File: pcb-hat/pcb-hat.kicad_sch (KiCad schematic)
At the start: 42 parts, among them U1 INA219AxD, U2 AOZ6605PI-1, U3 HTD Servo, U4 Vertical_Pi_Breakout, U5 Raspberry_Pi_Generic, U6 Power_Connector, U7 LM1084ISX-5.0_NOPB, U8 Horizontal_Pi_Breakout

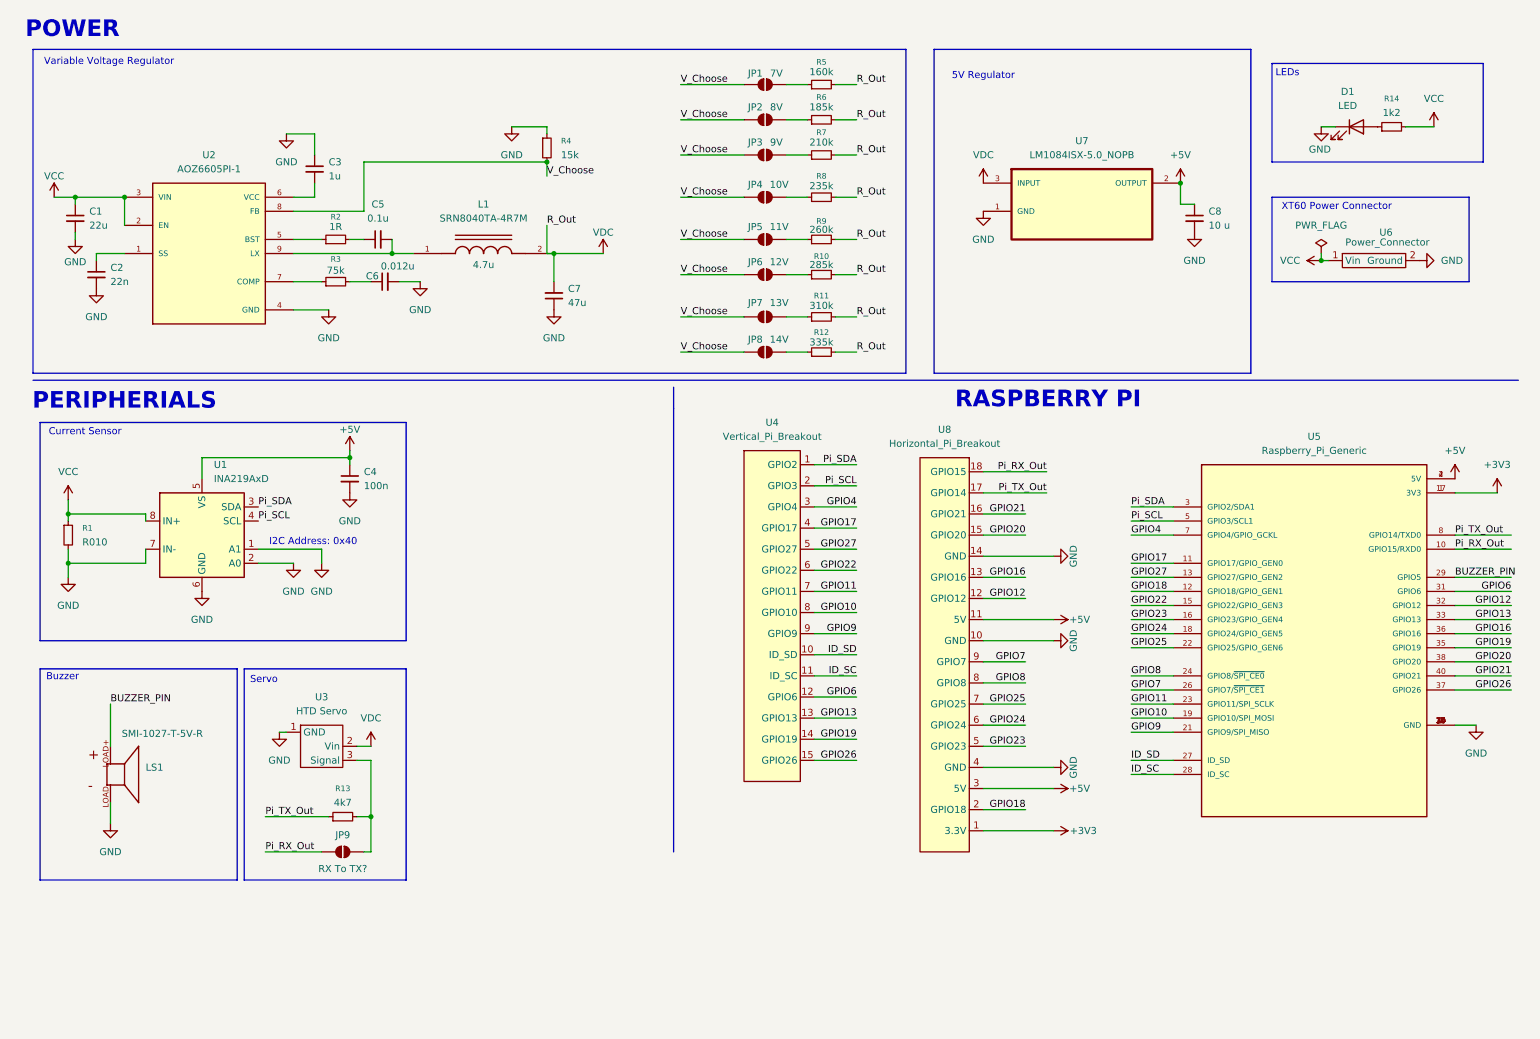
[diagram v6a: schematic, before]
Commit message: Don't short pwr to gnd for current sensor
Also use higher power rating for shunt
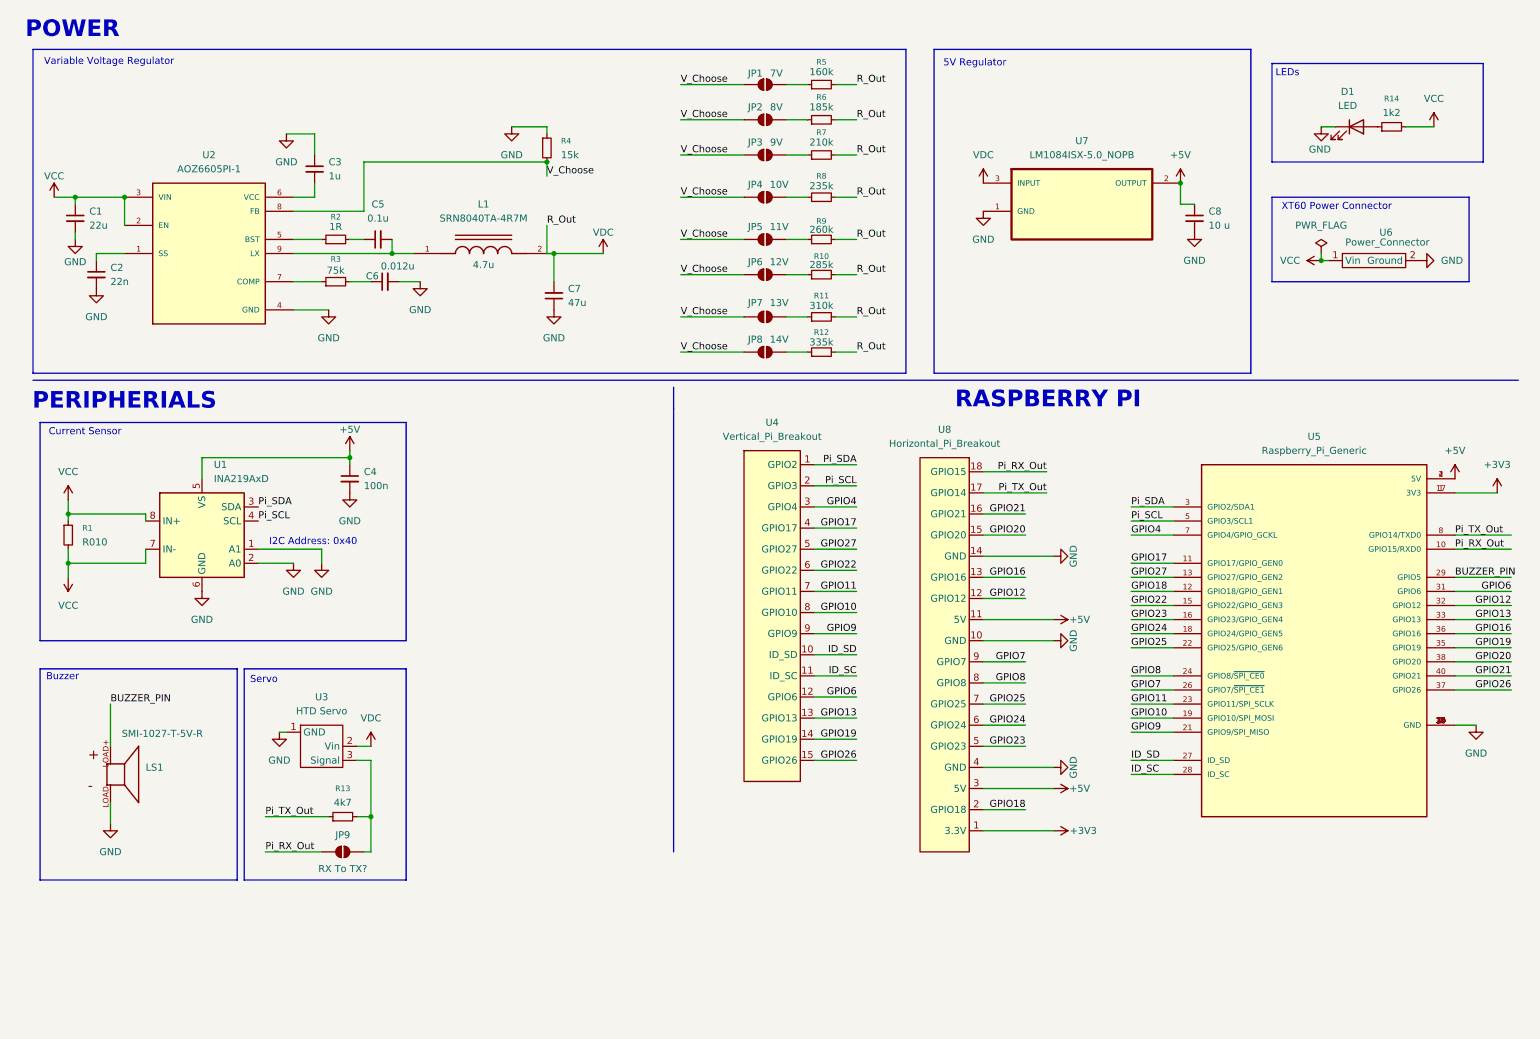
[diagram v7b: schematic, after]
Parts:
- R1: Digikey https://www.digikey.com/en/products/detail/susumu/RL0816T-R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 -> https://www.digikey.com/en/products/detail/yageo/PE0603FRE5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
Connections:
- net GND: no longer R1.2, U1.7 (IN-)
- net VCC: now also R1.2, U1.7 (IN-)
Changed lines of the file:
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@@
 	(text "5V Regulator\n"
 		(exclude_from_sim no)
-		(at 185.42 23.876 0)
+		(at 183.896 21.59 0)
 		(effects
 			(font
@@
 			)
 		)
-		(property "Datasheet" "https://www.susumu.co.jp/common/pdf/n_catalog_partition08_en.pdf"
+		(property "Datasheet" "https://mm.digikey.com/Volume0/opasdata/d220001/medias/docus/5343/PE_Series_DS.pdf"
 			(at 20.32 106.68 0)
 			(effects
@@
 			)
 		)
-		(property "Digikey" "https://www.digikey.com/en/products/detail/susumu/RL0816T-R010-F/2734741"
+		(property "Digikey" "https://www.digikey.com/en/products/detail/yageo/PE0603FRE570R01Z/17009517"
 			(at 20.32 106.68 0)
 			(effects
@@
 	)
 	(symbol
+		(lib_id "power:VCC")
+		(at 20.32 114.3 180)
+		(unit 1)
+		(exclude_from_sim no)
+		(in_bom yes)
+		(on_board yes)
+		(dnp no)
+		(fields_autoplaced yes)
+		(property "Reference" "#PWR03"
+			(at 20.32 110.49 0)
+			(effects
+				(font
+					(size 1.27 1.27)
+				)
+				(hide yes)
+			)
+		)
+		(property "Value" "VCC"
+			(at 20.32 119.38 0)
+			(effects
+				(font
+					(size 1.27 1.27)
+				)
+			)
+		)
+		(property "Footprint" ""
+			(at 20.32 114.3 0)
+			(effects
+				(font
+					(size 1.27 1.27)
+				)
+				(hide yes)
+			)
+		)
+		(property "Datasheet" ""
+			(at 20.32 114.3 0)
+			(effects
+				(font
+					(size 1.27 1.27)
+				)
+				(hide yes)
+			)
+		)
+		(property "Description" "Power symbol creates a global label with name \"VCC\""
+			(at 20.32 114.3 0)
+			(effects
+				(font
+					(size 1.27 1.27)
+				)
+				(hide yes)
+			)
+		)
+		(pin "1"
+		)
+		(instances
+			(project ""
+				(path "/a3c2d30d-0751-4de7-a899-3d89ad40795d"
+					(reference "#PWR03")
+					(unit 1)
+				)
+			)
+		)
+	)
+	(symbol
 		(lib_id "Device:C_Small")
 		(at 77.47 60.96 90)
@@
 					(unit 1)
 				)
-			)
-		)
-	)
-	(symbol
-		(lib_id "power:GND")
-		(at 20.32 114.3 0)
-		(unit 1)
-		(exclude_from_sim no)
-		(in_bom yes)
-		(on_board yes)
-		(dnp no)
-		(fields_autoplaced yes)
-		(property "Reference" "#PWR03"
-			(at 20.32 120.65 0)
-			(effects
-				(font
-					(size 1.27 1.27)
-				)
-				(hide yes)
-			)
-		)
-		(property "Value" "GND"
-			(at 20.32 119.38 0)
-			(effects
-				(font
-					(size 1.27 1.27)
-				)
-			)
-		)
-		(property "Footprint" ""
-			(at 20.32 114.3 0)
-			(effects
-				(font
-					(size 1.27 1.27)
-				)
-				(hide yes)
-			)
-		)
-		(property "Datasheet" ""
-			(at 20.32 114.3 0)
-			(effects
-				(font
-					(size 1.27 1.27)
-				)
-				(hide yes)
-			)
-		)
-		(property "Description" "Power symbol creates a global label with name \"GND\" , ground"
-			(at 20.32 114.3 0)
-			(effects
-				(font
-					(size 1.27 1.27)
-				)
-				(hide yes)
-			)
-		)
-		(pin "1"
-		)
-		(instances
-			(project ""
-				(path "/a3c2d30d-0751-4de7-a899-3d89ad40795d"
-					(reference "#PWR03")
-					(unit 1)
-				)

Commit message: Add mosfets, new led, and cleanup schematic some more
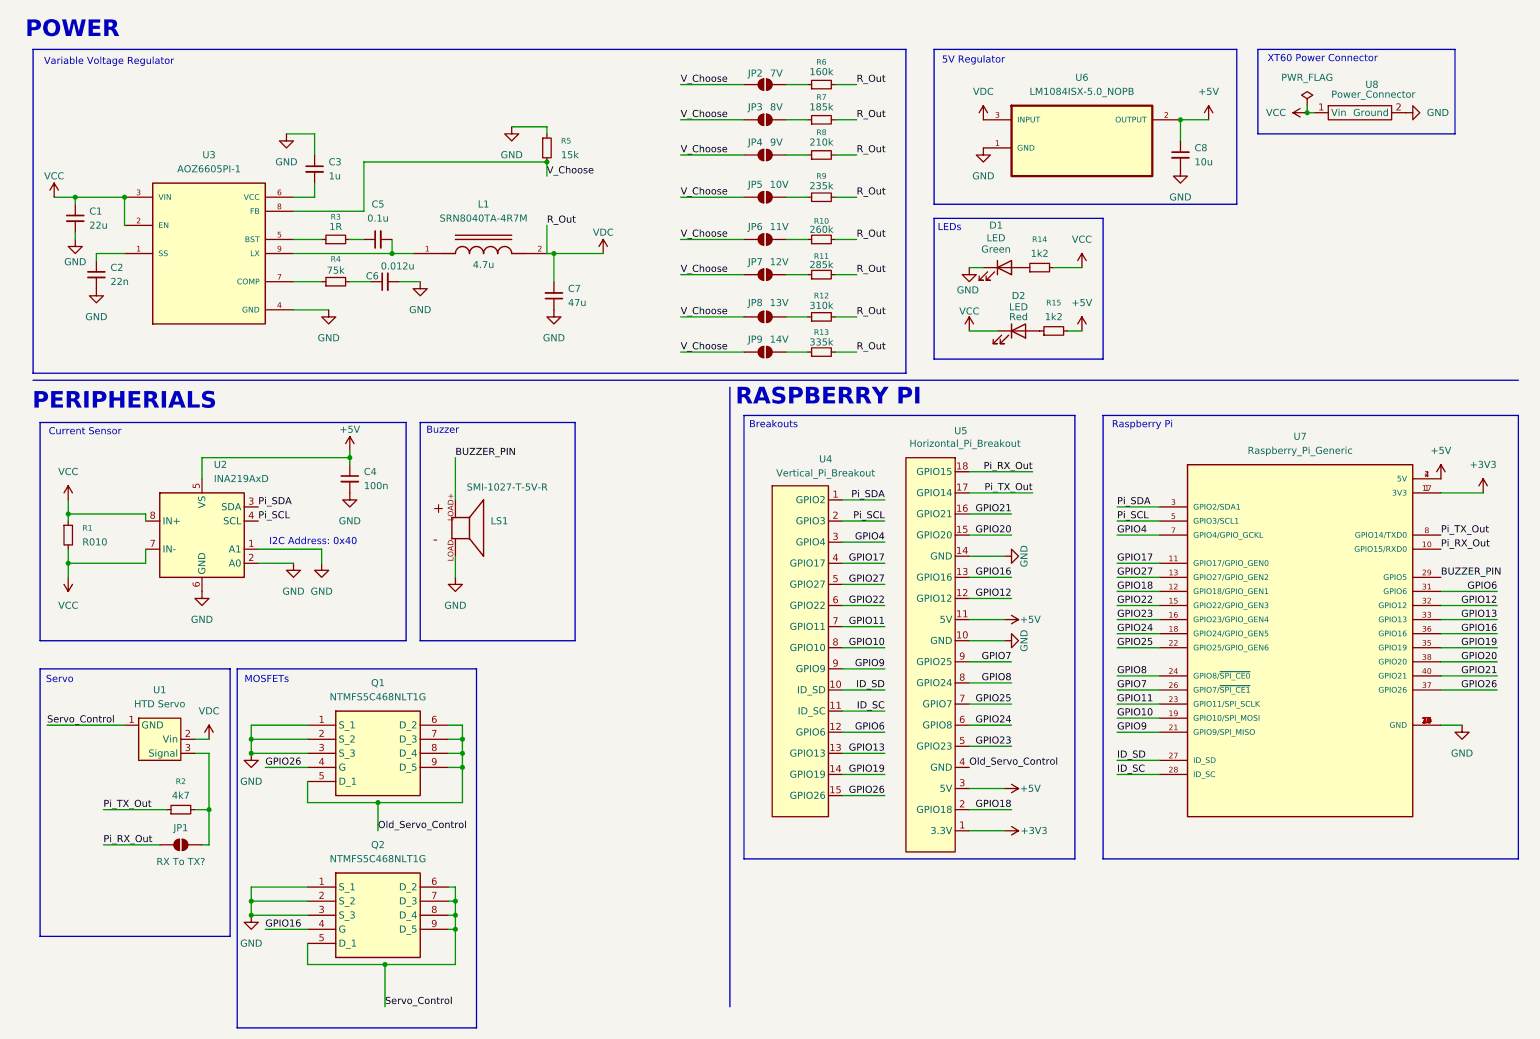
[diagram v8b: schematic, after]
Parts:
- added D2: LED, symbol Device:LED
- added Q1, Q2: NTMFS5C468NLT1G, pcb_hat:NRVTS10100EMFST1G, symbol PiHatComponents:NTMFS5C468NLT1G
- added R15: 1k2, Resistor_SMD:R_0603_1608Metric_Pad0.98x0.95mm_HandSolder, symbol Device:R_Small
- C8: value 10 u -> 10u; footprint (none) -> Capacitor_SMD:C_0603_1608Metric_Pad1.08x0.95mm_HandSolder; Digikey Link (none) -> https://www.digikey.com/en/products/detail/samsung-electro-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
- D1: Color (none) -> Green
- U6: renamed from U7; footprint LM1084ISX-5.0_NOPB:TO254P1524X483-4N -> pcb_hat:TO254P1524X483-4N; Digikey Link (none) -> https://www.digikey.com/en/products/detail/texas-instrument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
- U8: renamed from U6; footprint pi_hat:XT60 -> pcb_hat:XT60
- renumbered JP9 to JP1, JP1 to JP2, JP2 to JP3, JP3 to JP4, JP4 to JP5, JP5 to JP6, JP6 to JP7, JP7 to JP8, JP8 to JP9, R9 to R10, R10 to R11, R11 to R12, R12 to R13, R13 to R2, R2 to R3, R3 to R4, R4 to R5, R5 to R6, R6 to R7, R7 to R8, R8 to R9, U3 to U1, U1 to U2, U2 to U3, U8 to U5, U5 to U7
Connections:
- net +5V: now also R15.2
- net GND: now also Q1.1 (S_1), Q1.2 (S_2), Q1.3 (S_3), Q2.1 (S_1), Q2.2 (S_2), Q2.3 (S_3); no longer U1.1 (GND), U5.4 (GND)
- net GPIO16: now also Q2.4 (G)
- net GPIO26: now also Q1.4 (G)
- net VCC: now also D2.1 (K)
- new net: D2.2 (A), R15.1
- new net Old_Servo_Control: Q1.5 (D_1), Q1.6 (D_2), Q1.7 (D_3), Q1.8 (D_4), Q1.9 (D_5), U5.4 (GND)
- new net Servo_Control: Q2.5 (D_1), Q2.6 (D_2), Q2.7 (D_3), Q2.8 (D_4), Q2.9 (D_5), U1.1 (GND)
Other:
- note added: "Breakouts"
- note added: "MOSFETs"
- note added: "Raspberry Pi"
- moved on the sheet: C8, D1, JP1, LS1, R14, R2, U4, U5, U6, U7, U8
